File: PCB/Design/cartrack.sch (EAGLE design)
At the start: 37 parts, among them J1 POWER_JACKPTH, Q4 12MHz, Q5 LM2941, U1 ATMEGA644P-20AU

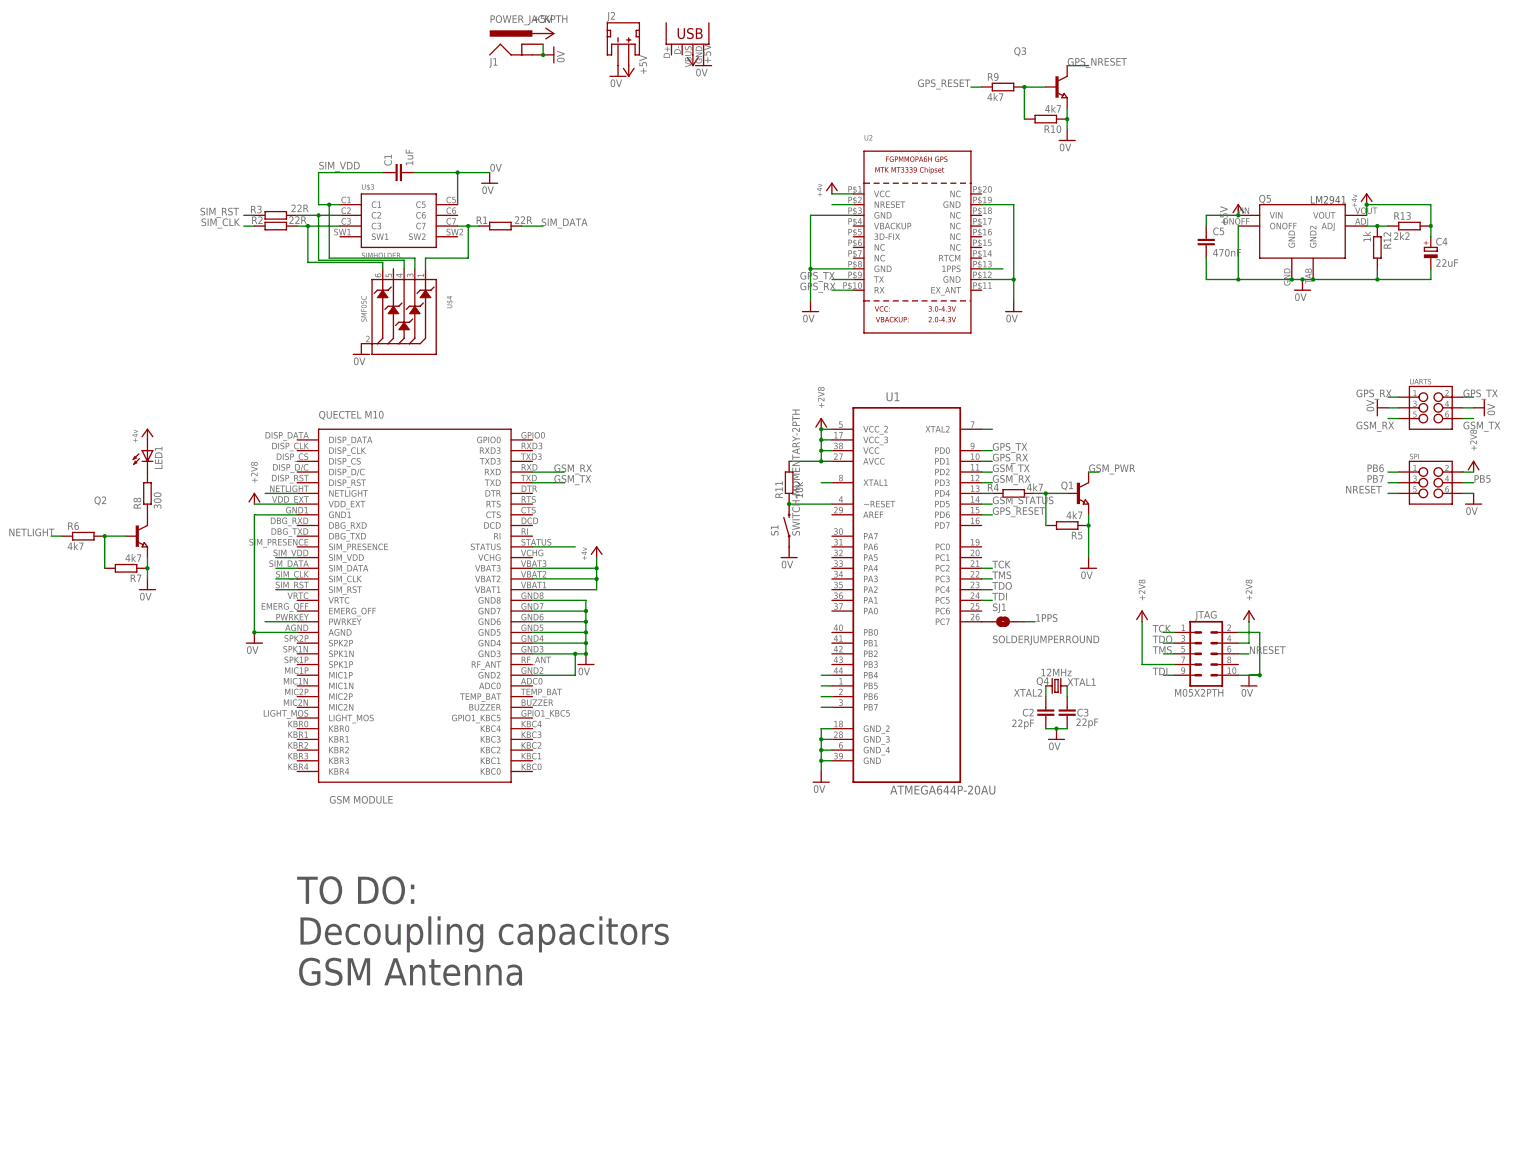
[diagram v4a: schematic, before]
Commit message: Finished schematic.
Started on PCB.
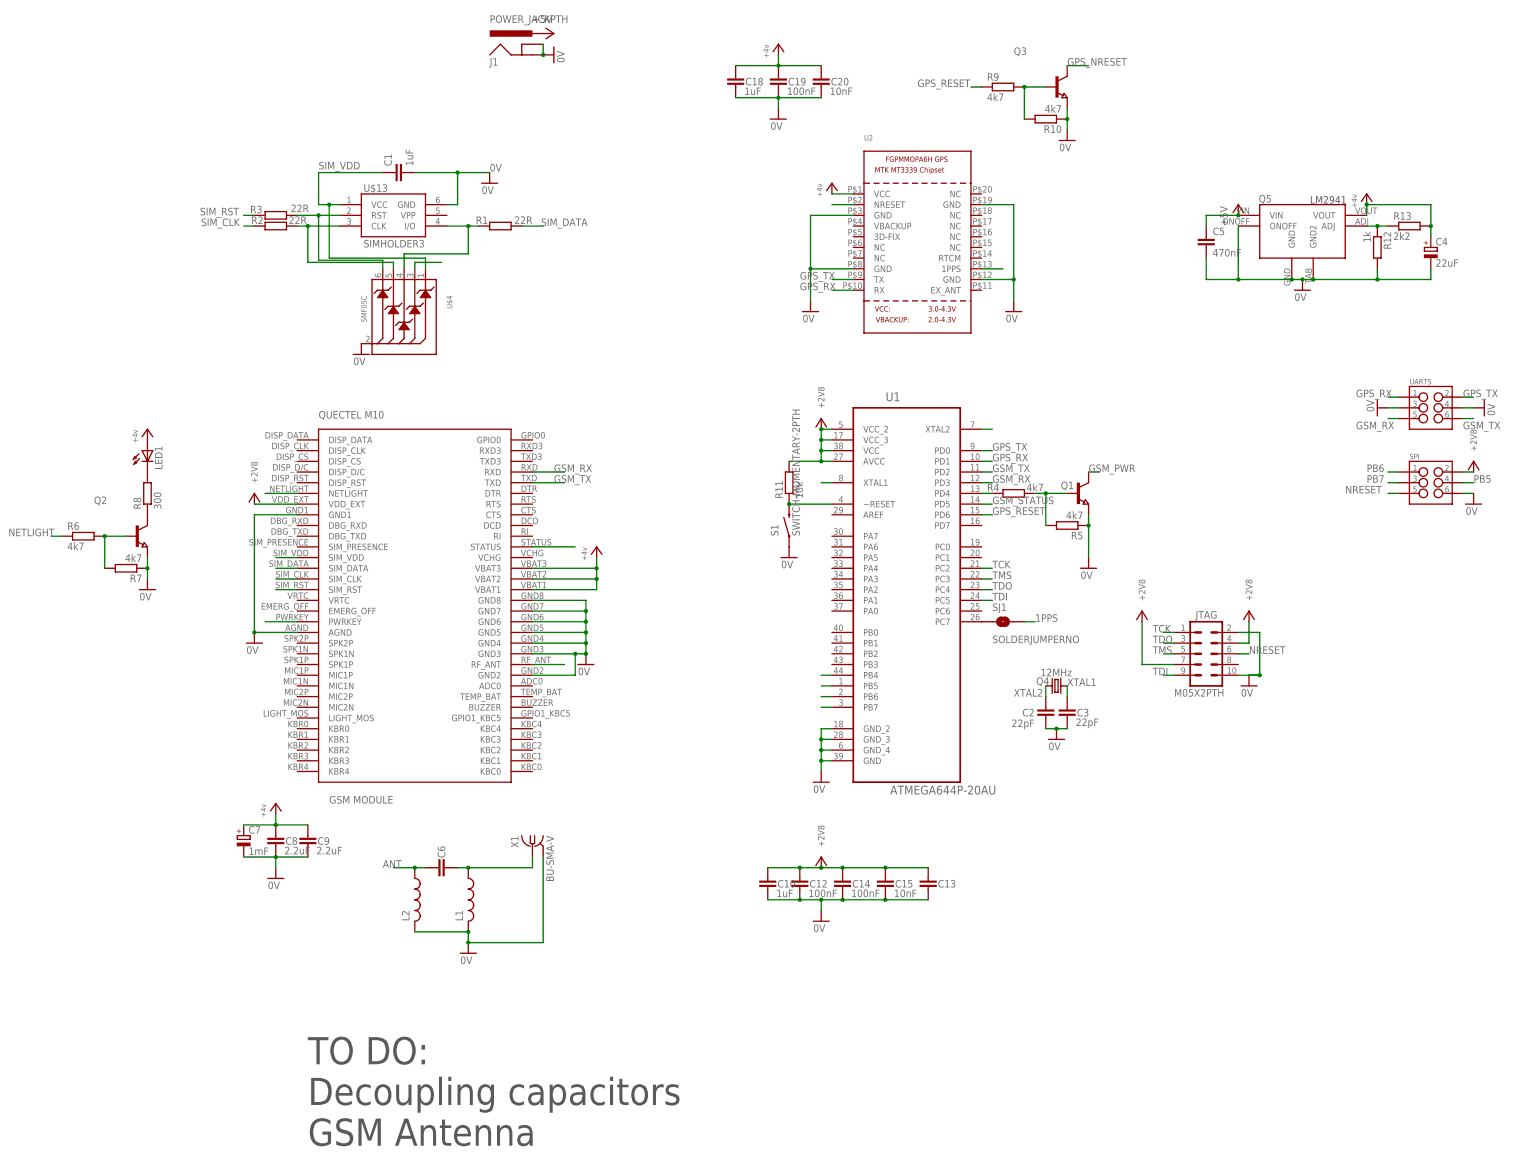
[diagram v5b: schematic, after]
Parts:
- removed J2: (no value), SparkFun-Connectors:JST_2MM_MALE
- removed JP1: USBSMD, SparkFun-Connectors:USBSMD
- removed U$3: SIMHOLDER, SparkFun-Connectors:SIMHOLDER
- added C10, C18: 1uF, SparkFun-Passives:CAPPTH
- added C12, C14, C19: 100nF, SparkFun-Passives:CAP1206
- added C13, C6: (no value), SparkFun-Passives:CAP0603-CAP
- added C15, C20: 10nF, SparkFun-Passives:CAP0603-CAP
- added C7: 1mF, resistor:CPOL-EUE3.5-8
- added C8, C9: 2.2uF, SparkFun-Passives:CAP1206
- added L1, L2: (no value), resistor:L-USL2012C
- added U$13: SIMHOLDER3, SparkFun-Connectors:SIMHOLDER3
- added X1: BU-SMA-V, con-coax:BU-SMA-V
- SJ1: value SOLDERJUMPERROUND -> SOLDERJUMPERNO; device SparkFun-Retired:SOLDERJUMPERROUND -> SparkFun-Retired:SOLDERJUMPERNO
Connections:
- new net ANT: C6.1, L2.1, U$1.RF_ANT
- new net N$14: C6.2, L1.1, X1.1
- net +2V8: now also C10.1, C12.1, C13.1, C14.1, C15.1
- net +4V: now also C18.1, C19.1, C20.1, C7.+, C8.1, C9.1
- net +5V: no longer J2.+, JP1.VBUS
- net 0V: now also C10.2, C12.2, C13.2, C14.2, C15.2, C18.2, C19.2, C20.2, C7.-, C8.2, C9.2, L1.2, L2.2, U$13.GND, X1.2; no longer J2.-, JP1.GND, U$3.C5
- net GSM_PWR: now also U$4.CATODE2
- net N$1: now also U$13.I/O, U$4.CATODE3; no longer U$3.C7, U$4.CATODE1
- net N$2: now also U$13.CLK, U$4.CATODE4; no longer U$3.C3, U$4.CATODE5
- net N$3: now also U$13.RST, U$4.CATODE5; no longer U$3.C2, U$4.CATODE3
- net SIM_VDD: now also U$13.VCC, U$4.CATODE1; no longer U$3.C1, U$4.CATODE2

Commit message: Redone the PCB layout. Corrected mask and pad errors in the libraries
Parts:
- removed C10: 1uF, SparkFun-Passives:CAPPTH
- removed C14: 100nF, SparkFun-Passives:CAP1206
- removed UARTS: (no value), SparkFun-Connectors:M03X2NO_SILK
- added C11: 1uF, SparkFun-Passives:CAP1206
- added C16: 2.2uF, SparkFun-Passives:CAP1206
- added GPS, GSM: M02PTH, SparkFun-Connectors:M02PTH
- added Q6: TPS70928, misc:TPS70928
- renumbered LED1 to LED, SPI to ISP
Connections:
- net N$1 renamed SIM_DATA_R
- net N$14 renamed ANT_1
- net N$2 renamed SIM_CLK_R
- net N$3 renamed SIM_RST_R
- removed net 0V: C1.2, C10.2, C12.2, C13.2, C14.2, C15.2, C18.2, C19.2, C2.2, C20.2, C3.2, C4.-, C5.2, C7.-, C8.2, C9.2, ISP.6, J1.GND, J1.GNDBREAK, JTAG.10, JTAG.2, L1.2, L2.2, Q1.E, Q2.E, Q3.E, Q5.GND, Q5.GND2, Q5.ONOFF, R10.1, R12.2, R5.1, R7.1, S1.1, U$1.AGND, U$1.GND1, U$1.GND2, U$1.GND3, U$1.GND4, U$1.GND5, U$1.GND6, U$1.GND7, U$1.GND8, U$13.GND, U$4.ANODE, U1.GND, U1.GND_2, U1.GND_3, U1.GND_4, U2.GND@1, U2.GND@2, U2.GND@3, U2.GND@4, UARTS.3, UARTS.4, X1.2
- removed net PB4: U1.PB4
- new net GND: C1.2, C11.2, C12.2, C13.2, C15.2, C16.2, C18.2, C19.2, C2.2, C20.2, C3.2, C4.-, C5.2, C7.-, C8.2, C9.2, ISP.6, J1.GND, J1.GNDBREAK, JTAG.10, JTAG.2, L1.2, L2.2, Q1.E, Q2.E, Q3.E, Q5.GND, Q5.ONOFF, Q6.GND, R10.1, R12.2, R5.1, R7.1, S1.1, U$1.AGND, U$1.GND1, U$1.GND2, U$1.GND3, U$1.GND4, U$1.GND5, U$1.GND6, U$1.GND7, U$1.GND8, U$13.GND, U$4.ANODE, U2.GND@1, U2.GND@2, U2.GND@3, U2.GND@4, X1.2
- net +2V8: now also C16.1, Q6.VOUT; no longer C10.1, C14.1, U$1.VDD_EXT, U1.AVCC, U1.VCC_2, U1.VCC_3
- net +4V: now also C11.1, Q6.VIN
- net GPS_RX: now also GPS.1; no longer UARTS.1
- net GPS_TX: now also GPS.2; no longer UARTS.2
- net GSM_RX: now also GSM.1; no longer UARTS.5
- net GSM_TX: now also GSM.2; no longer UARTS.6
- net N$13: now also U1.PB3; no longer U1.PC7
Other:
- note removed: "TO DO: Decoupling capacitors GSM Antenna"
- moved on the sheet: R11, S1, SJ1
